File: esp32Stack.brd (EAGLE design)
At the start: 31.5 x 30 mm, 23 parts, among them J02 470, J04 470, J05 470, J12 470, J13 470

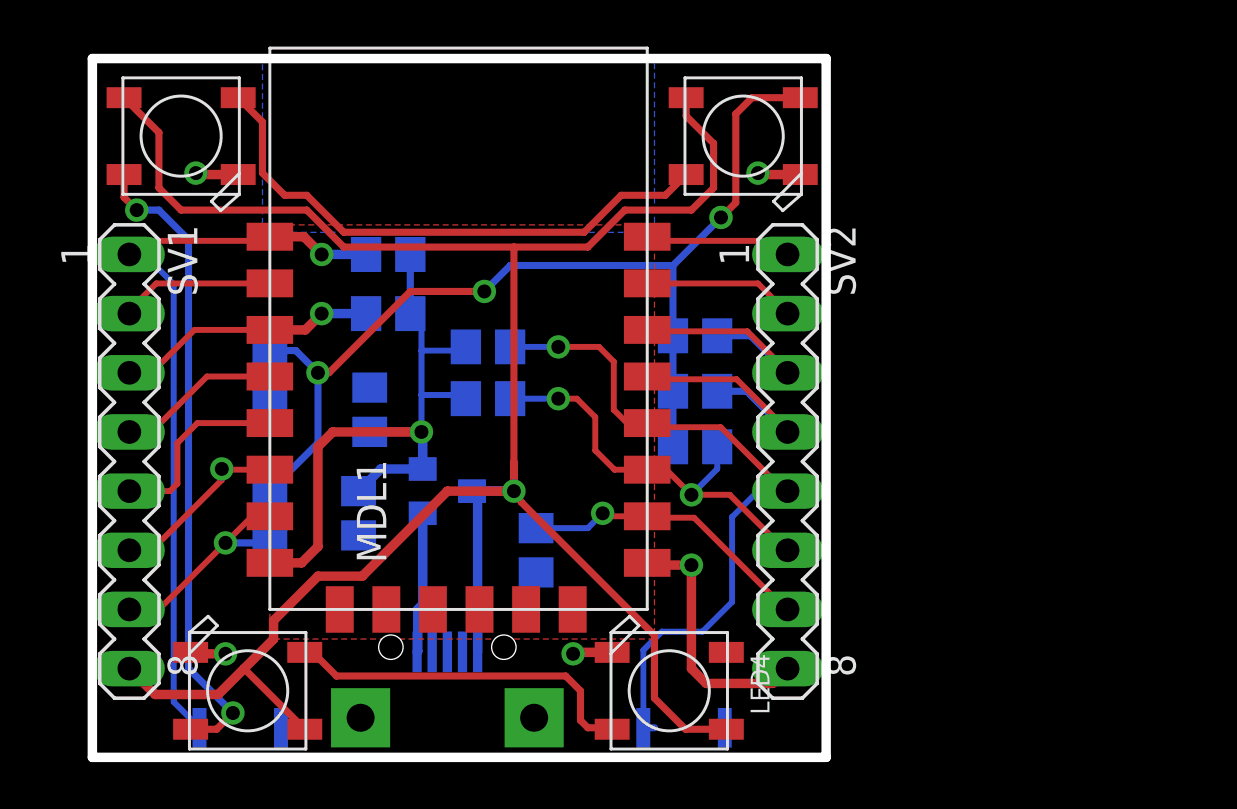
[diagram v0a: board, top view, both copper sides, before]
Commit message: added an ftdi version
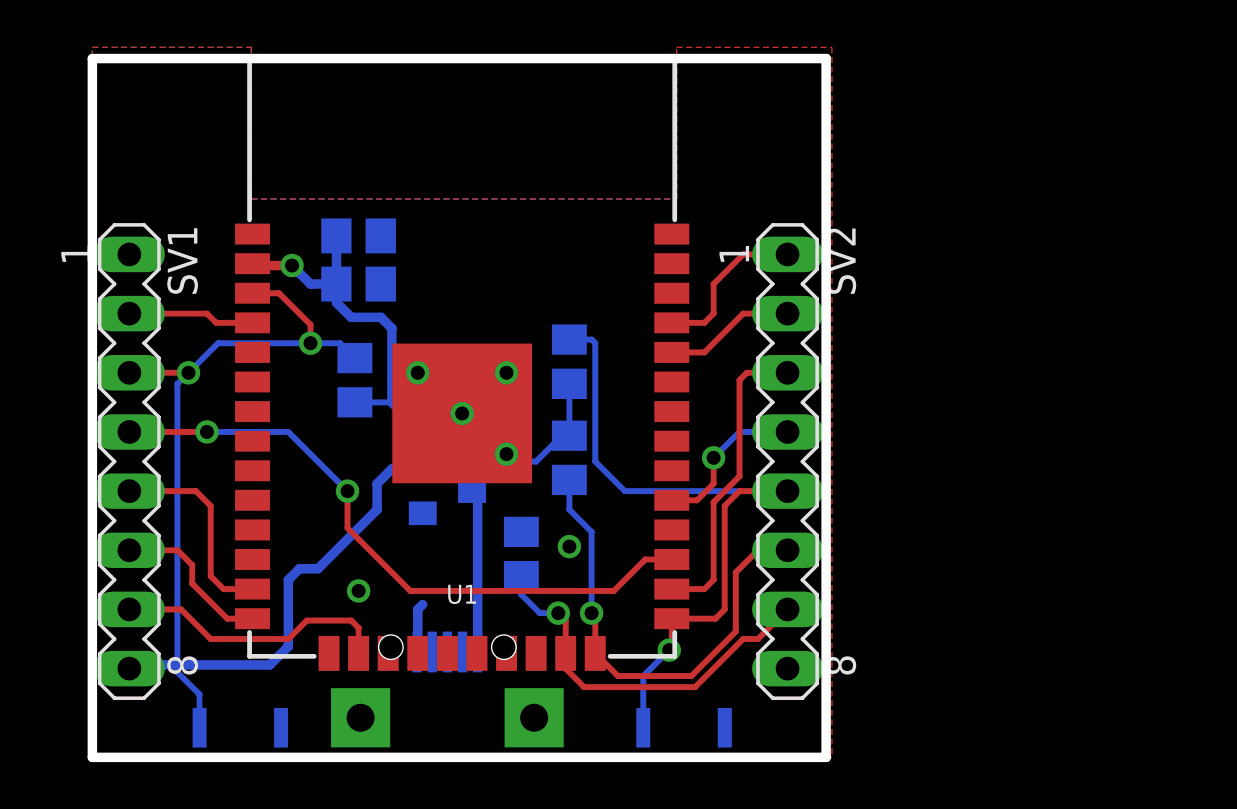
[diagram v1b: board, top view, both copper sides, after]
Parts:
- removed J02, J04, J05, J12, J13: 470, eagle-ltspice:R0805
- removed LED1, LED2, LED3, LED4: WS2812B5050, adafruit:WS2812B
- removed MDL1: (no value), ESP12E:ESP8266-ESP12E
- removed R1: 10k, eagle-ltspice:R0805
- added U1: ESP-WROOM-03, esp32:ESP-WROOM-03
- moved C1 9.84 mm to (11.4, 20.3), turned to 180 degrees
- moved C2 7.48 mm to (11.4, 22.4), turned to 180 degrees
- moved R3 4.32 mm to (20.5, 12.9), turned to 90 degrees
- moved R4 3.55 mm to (20.5, 17.0), turned to 270 degrees
- moved R2 3.19 mm to (11.3, 16.2), turned to 270 degrees
- moved R5 0.65 mm to (18.4, 8.73), turned to 270 degrees
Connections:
- removed net 3V3: C1.1, C2.1, GND.2, MDL1.8, R1.2, R2.2, R3.2, R4.2
- removed net 5V: GND.3, LED1.1-VDD, LED2.1-VDD, LED3.1-VDD, LED4.1-VDD, SV1.8, U$2.1
- removed net CH_PD: MDL1.3, R2.1, SV1.3
- removed net DIN: J02.1, J04.1, J05.1, J12.1, J13.1, LED1.4-DIN
- removed net DOUT1DIN2: LED1.2-DOUT, LED2.4-DIN
- removed net DOUT2DIN3: LED2.2-DOUT, LED3.4-DIN
- removed net DOUT3DIN4: LED3.2-DOUT, LED4.4-DIN
- removed net GPIO16: MDL1.4, SV1.4
- removed net REST: MDL1.1, R1.1, REST.1, SV1.1
- removed net RXD: MDL1.15, SV2.2
- removed net TXD: MDL1.16, SV2.1
- new net EN: R2.1, REST.1, SV1.3, U1.3
- new net N$1: SV2.1, U1.35
- new net N$2: SV2.2, U1.34
- new net N$3: SV1.5, U1.13
- new net N$4: GND.3, U$2.1
- new net VCC/V3.3: C1.1, C2.1, GND.2, R2.2, R3.2, R4.2, SV1.8, U1.2
- net ADC: now also U1.4; no longer MDL1.2
- net GND: now also U1.1, U1.15, U1.38, U1.5, U1.GND; no longer LED1.3-GND, LED2.3-GND, LED3.3-GND, LED4.3-GND, MDL1.9
- net GPIO0: now also U1.25; no longer MDL1.12
- net GPIO12: now also U1.14; no longer J12.2, MDL1.6
- net GPIO13: now also U1.16; no longer J13.2, MDL1.7
- net GPIO14: now also SV1.4, U1.27; no longer MDL1.5, SV1.5
- net GPIO15: now also U1.23; no longer MDL1.10
- net GPIO2: now also U1.24; no longer J02.2, MDL1.11
- net GPIO4: now also U1.29; no longer J04.2, MDL1.13
- net GPIO5: now also U1.26; no longer J05.2, MDL1.14
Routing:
- net 5V: track 95.0 -> 0.00 mm, vias 1 -> 0
- net VCC/V3.3: track 0.00 -> 45.5 mm, vias 0 -> 1
- net DIN: track 44.5 -> 0.00 mm, vias 3 -> 0
- net REST: track 32.8 -> 0.00 mm, vias 1 -> 0
- net EN: track 0.00 -> 30.1 mm, vias 0 -> 2
- net 3V3: track 29.8 -> 0.00 mm, vias 1 -> 0
- net DOUT2DIN3: track 27.7 -> 0.00 mm, vias 2 -> 0
- net DOUT1DIN2: track 23.9 -> 0.00 mm
- net GND: track 24.0 -> 2.13 mm, vias 5 -> 6
- net GPIO14: track 8.46 -> 27.6 mm, vias 0 -> 2
- net DOUT3DIN4: track 15.3 -> 0.00 mm
- net CH_PD: track 11.4 -> 0.00 mm, vias 1 -> 0
- net N$3: track 0.00 -> 8.80 mm
- net GPIO16: track 7.27 -> 0.00 mm
- net N$4: track 0.00 -> 7.00 mm
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- added copper zone on layer 1, net GND
- removed copper zone on layer 1, net 5V

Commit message: FT232 module
FT232 Module now functional as a prototype
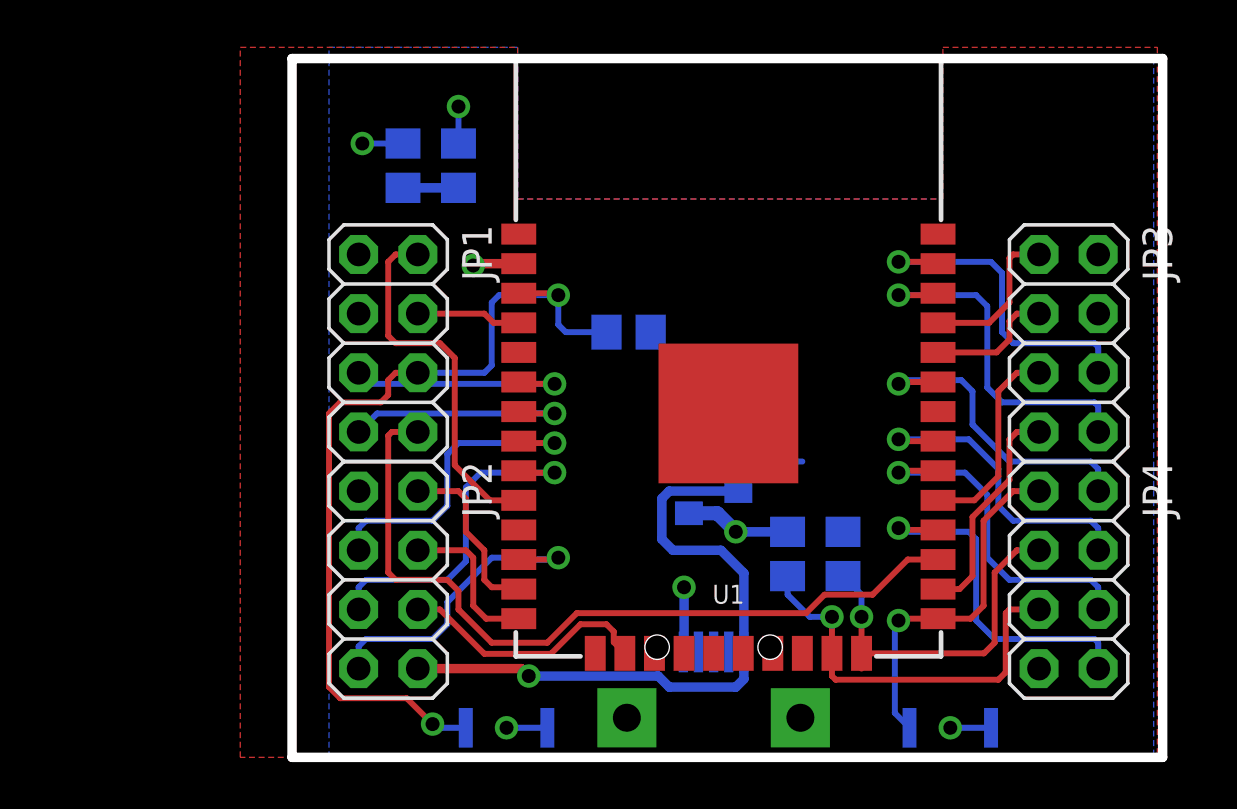
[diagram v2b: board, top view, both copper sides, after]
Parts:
- removed R4: 10k, eagle-ltspice:R0805
- removed SV1, SV2: (no value), con-lstb:MA08-1
- added JP1, JP2, JP3, JP4: (no value), adafruit:2X04
- moved R3 12.5 mm to (32.2, 8.73)
- moved R2 11.9 mm to (23.0, 18.3), turned to 180 degrees
- moved GND 11.4 mm to (26.7, 11.4)
- moved REST 11.4 mm to (17.8, 1.27)
- moved U$2 11.4 mm to (26.7, 0.00)
- moved FLASH 11.4 mm to (36.8, 1.27)
- moved R5 11.4 mm to (29.8, 8.73)
- moved U1 11.4 mm to (27.3, 14.8)
- moved C1 5.43 mm to (13.3, 25.4), turned to 90 degrees
- moved C2 5.24 mm to (15.7, 25.4), turned to 90 degrees
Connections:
- removed net N$1: SV2.1, U1.35
- removed net N$2: SV2.2, U1.34
- removed net N$3: SV1.5, U1.13
- removed net N$4: GND.3, U$2.1
- removed net VCC/V3.3: C1.1, C2.1, GND.2, R2.2, R3.2, R4.2, SV1.8, U1.2
- new net +5V: GND.3, JP2.8, U$2.1
- new net 3V3: C1.1, C2.1, GND.2, R2.2, R3.2, U1.2
- new net GPIO16: JP1.8, U1.27
- new net GPIO17: JP4.8, U1.28
- new net GPIO18: JP4.6, U1.30
- new net GPIO19: JP4.4, U1.31
- new net GPIO21: JP4.2, U1.33
- new net GPIO22: JP3.8, U1.36
- new net GPIO23: JP3.6, U1.37
- new net GPIO25: JP1.2, U1.10
- new net GPIO27: JP2.7, U1.12
- new net GPIO32: JP2.3, U1.8
- new net GPIO33: JP2.5, U1.9
- new net GPIO34: JP1.5, U1.6
- new net GPIO35: JP1.7, U1.7
- new net RXD: JP3.3, U1.34
- new net TXD: JP3.1, U1.35
- net ADC: now also JP1.4; no longer SV1.2
- net EN: now also JP1.6; no longer SV1.3
- net GND: now also JP4.7; no longer SV2.8
- net GPIO0: now also JP4.1; no longer R4.1, SV2.5
- net GPIO12: now also JP2.4; no longer SV1.6
- net GPIO13: now also JP2.6; no longer SV1.7
- net GPIO14: now also JP2.2, U1.13; no longer SV1.4, U1.27
- net GPIO15: now also JP4.5; no longer SV2.7
- net GPIO2: now also JP4.3; no longer SV2.6
- net GPIO4: now also JP3.7, U1.26; no longer SV2.4, U1.29
- net GPIO5: now also JP3.5, U1.29; no longer SV2.3, U1.26
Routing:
- net VCC/V3.3: track 45.5 -> 0.00 mm, vias 1 -> 0
- net GPIO16: track 0.00 -> 34.0 mm
- net +5V: track 0.00 -> 28.3 mm, vias 0 -> 1
- net GPIO14: track 27.6 -> 7.66 mm, vias 2 -> 0
- net GPIO25: track 0.00 -> 15.9 mm
- net GPIO17: track 0.00 -> 15.5 mm, vias 0 -> 1
- net GPIO22: track 0.00 -> 15.4 mm, vias 0 -> 1
- net GPIO18: track 0.00 -> 14.9 mm, vias 0 -> 1
- net GPIO33: track 0.00 -> 14.8 mm, vias 0 -> 1
- net GPIO23: track 0.00 -> 14.4 mm, vias 0 -> 1
- net GPIO0: track 30.1 -> 15.9 mm
- net GPIO32: track 0.00 -> 14.0 mm, vias 0 -> 1
- net GPIO19: track 0.00 -> 13.8 mm, vias 0 -> 1
- net GPIO21: track 0.00 -> 13.7 mm, vias 0 -> 1
- net GPIO27: track 0.00 -> 13.7 mm, vias 0 -> 1
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- added copper zone on layer 16, net 3V3
- removed copper zone on layer 16, net GND
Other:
- board size 31.5 x 30 mm -> 37.4 x 30 mm
